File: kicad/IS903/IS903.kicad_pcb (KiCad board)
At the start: 4 copper layers, 33 x 14 mm, 31 parts, among them J1 USB3_A, U1 IS903_QFN64_8*8, U2 EML3020, U3 EMP8733-1.2, U4 NAND_BGA152, U5 NAND_BGA152, Y1 30MHZ 2520

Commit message: 2020.7.23
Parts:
- moved R8 3.02 mm to (132.5, 94.4)
- moved R7 2.92 mm to (132.5, 97.4)
- moved C11 0.60 mm to (111.5, 92.2)
- moved C8 0.60 mm to (108.3, 92.2)
- moved L1 0.60 mm to (111.6, 95.3)
- moved R1 0.60 mm to (109.4, 92.2)
- moved R2 0.60 mm to (110.4, 92.2)
- moved U2 0.60 mm to (109.0, 95.4)
- moved C7 0.41 mm to (107.5, 88.8)
- moved C9 0.30 mm to (107.0, 92.0)
- moved C5 0.20 mm to (111.2, 99.0)
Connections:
- U1 pad 30: Net-(U1-Pad30) -> (no net)
- U1 pad 31: Net-(U1-Pad31) -> (no net)
- U1 pad 32: Net-(U1-Pad32) -> (no net)
- U1 pad 5: Net-(U1-Pad5) -> (no net)
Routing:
- net /VSS1: track 0.00 -> 38.5 mm, vias 0 -> 1
- net /F0_IO3: track 0.00 -> 37.4 mm, vias 0 -> 3
- net /F0_IO0: track 0.00 -> 37.4 mm, vias 0 -> 4
- net /F0_IO1: track 0.00 -> 33.2 mm, vias 0 -> 4
- net /F0_IO5: track 0.00 -> 32.8 mm, vias 0 -> 4
- net /F0_IO2: track 0.00 -> 32.1 mm, vias 0 -> 4
- net /F0_IO4: track 0.00 -> 29.3 mm, vias 0 -> 3
- net +3V3: track 0.00 -> 27.7 mm, vias 0 -> 10
- net GND: track 0.00 -> 27.5 mm, vias 0 -> 13
- net Net-(R4-Pad1): track 0.00 -> 27.3 mm, vias 0 -> 2
- net /F0_IO6: track 0.00 -> 25.9 mm, vias 0 -> 3
- net /F0_IO7: track 0.00 -> 25.9 mm, vias 0 -> 3
- net /F1_IO5: track 0.00 -> 24.9 mm, vias 0 -> 2
- net /F1_IO4: track 0.00 -> 24.4 mm, vias 0 -> 2
- net /F1_IO7: track 0.00 -> 23.6 mm, vias 0 -> 2
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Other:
- rule via_min_drill: 0.00508 -> 0.2
- rule via_min_size: 0.01143 -> 0.45

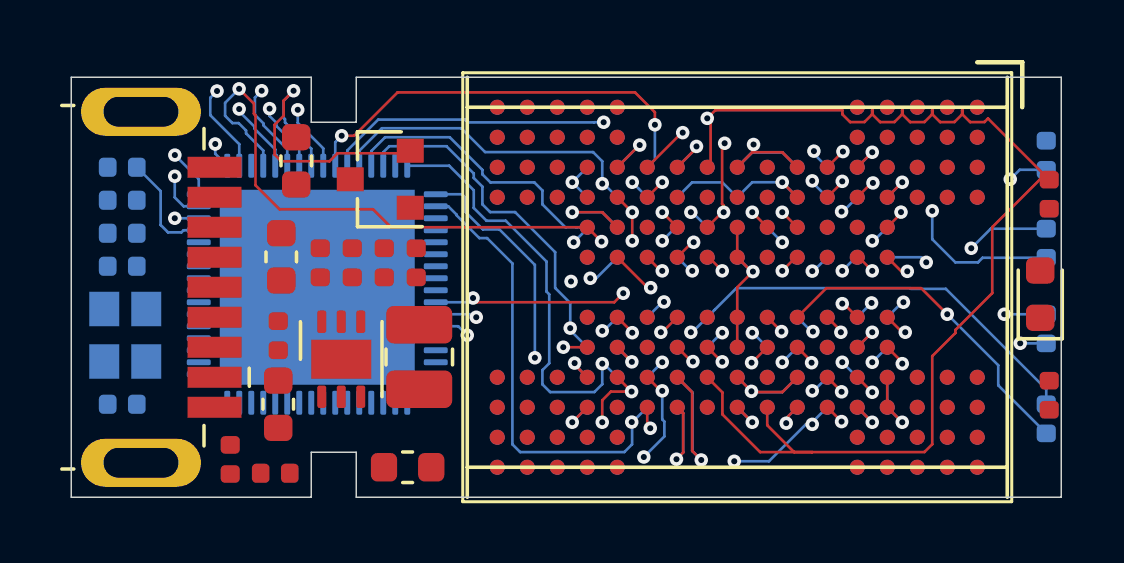
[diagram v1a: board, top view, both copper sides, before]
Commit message: 第一次布线失败，暂时放弃
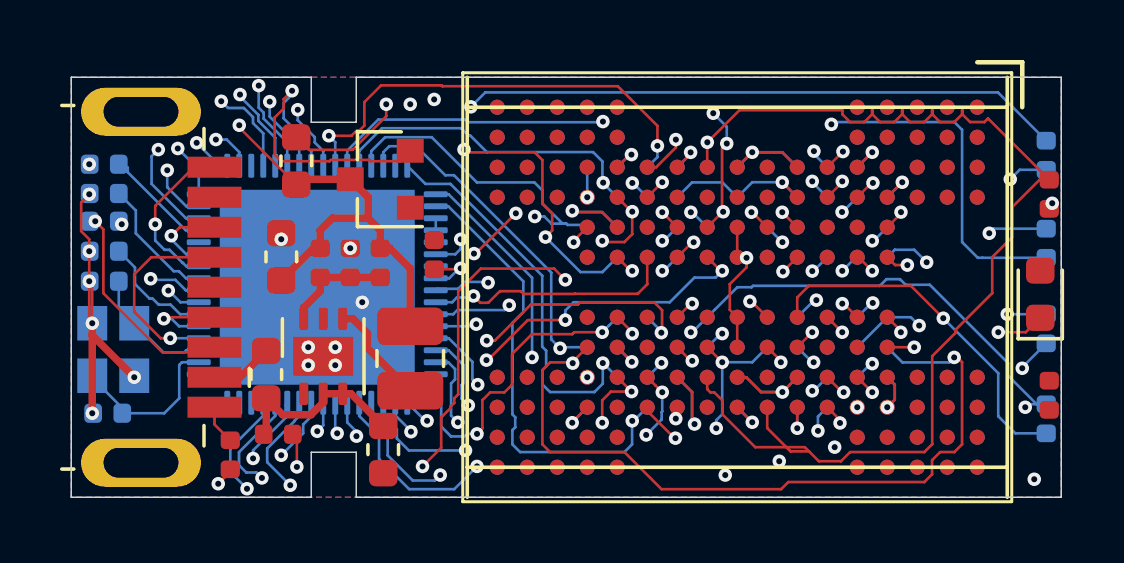
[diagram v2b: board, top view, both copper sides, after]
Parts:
- C1: moved to B.Cu
- moved C1 6.94 mm to (101.1, 90.8), turned to 180 degrees
- moved C3 1.30 mm to (106.9, 97.9)
- moved R2 1.13 mm to (109.3, 92.2)
- moved F1 1.07 mm to (106.5, 95.9)
- moved C5 1.00 mm to (110.4, 98.4), turned to 270 degrees
- moved R1 0.93 mm to (110.3, 92.2)
- moved C6 0.85 mm to (101.1, 91.8)
- moved C10 0.78 mm to (101.1, 92.8)
- moved C11 0.66 mm to (112.1, 91.9)
- moved C4 0.64 mm to (101.1, 89.9)
- moved Y1 0.62 mm to (101.4, 95.1)
- moved R3 0.61 mm to (101.1, 88.9)
- moved U2 0.61 mm to (108.4, 95.3)
- moved C12 0.57 mm to (101.2, 97.2)
- moved L1 0.30 mm to (111.3, 95.4)
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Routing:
- net +3V3: track 27.7 -> 80.9 mm, vias 10 -> 13
- net /F1_CE2n: track 12.2 -> 57.6 mm, vias 2 -> 4
- net /F1_CE3n: track 14.4 -> 51.2 mm, vias 1 -> 4
- net /F0_CE2n: track 10.4 -> 46.6 mm, vias 2 -> 3
- net /F0_CE3n: track 0.00 -> 35.8 mm, vias 0 -> 2
- net /F1_CE0n: track 0.74 -> 33.0 mm, vias 1 -> 3
- net /LED_0: track 0.00 -> 32.0 mm, vias 0 -> 2
- net /F1_CE1n: track 0.68 -> 29.6 mm, vias 1 -> 4
- net /F0_CE0n: track 3.11 -> 30.4 mm, vias 2 -> 4
- net /F0_CE1n: track 0.69 -> 20.0 mm, vias 1 -> 4
- net /F1_CLE: track 4.83 -> 24.1 mm, vias 2 -> 3
- net /F1_ALE: track 5.79 -> 24.1 mm, vias 2 -> 3
- net /F0_DQS: track 19.0 -> 35.8 mm, vias 4 -> 5
- net /F_WPn: track 5.41 -> 21.3 mm, vias 4 -> 5
- net /F1_WEn: track 7.77 -> 21.5 mm, vias 2 -> 4
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- added copper zone on VCC.Cu, net +3V3
- added copper zone on B.Cu, net GND
- added copper zone on F.Cu, net GND
- added copper zone on GND.Cu, net GND
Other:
- net class Default: clearance 0.2 -> 0.0889; trace_width 0.25 -> 0.0889
- rule trace_clearance: 0.2 -> 0.0889
